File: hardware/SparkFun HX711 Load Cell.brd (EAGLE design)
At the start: 30.5 x 22.9 mm, 26 parts, among them Q1 MMBT4403, U1 HX711, U7 OSHW-LOGOS

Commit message: Silk label adjustment. Added cnt for shielding (yellow).
Some load cells have a 5th wire that is yellow that shields the four
wires. Added a ground connection for this 5th wire.
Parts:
- removed JP3: (no value), SparkFun-Connectors:1X04
- removed SJ1: (no value), SparkFun-Passives:PAD-JUMPER-2-NO_YES_SILK
- added JP4: (no value), SparkFun-Connectors:1X05
- added SJ2: (no value), SparkFun-Passives:PAD-JUMPER-2-NC_BY_TRACE_YES_SILK
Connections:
- net A+: now also JP4.2; no longer JP3.1
- net A-: now also JP4.3; no longer JP3.2
- net AVDD: now also JP4.5; no longer JP3.4
- net GND: now also JP4.1, JP4.4, SJ2.1; no longer JP3.3, SJ1.1
- net N$1: now also SJ2.2; no longer SJ1.2
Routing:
- net A-: track 7.56 -> 8.09 mm
- net A+: track 9.20 -> 9.73 mm
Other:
- board text added: "V02"
- board text added: "YLW"
- board text added: "YLW/SD"
- board text removed: "V01"
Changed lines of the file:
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@@
 <wire x1="30.48" y1="0" x2="0" y2="0" width="0.2032" layer="20"/>
 <wire x1="0" y1="0" x2="0" y2="22.86" width="0.2032" layer="20"/>
-<text x="3.048" y="6.985" size="1.27" layer="21" font="vector" ratio="15">GRN</text>
+<text x="3.048" y="8.255" size="1.27" layer="21" font="vector" ratio="15">GRN</text>
 <text x="5.334" y="1.27" size="1.778" layer="21" font="vector" ratio="15">Load Cell Amp</text>
-<text x="3.048" y="12.065" size="1.27" layer="21" font="vector" ratio="15">BLK</text>
-<text x="3.048" y="9.525" size="1.27" layer="21" font="vector" ratio="15">WHT</text>
-<text x="3.048" y="14.605" size="1.27" layer="21" font="vector" ratio="15">RED</text>
-<text x="9.398" y="6.985" size="1.27" layer="22" font="vector" ratio="15" rot="MR0">GRN/A+</text>
-<text x="9.398" y="9.525" size="1.27" layer="22" font="vector" ratio="15" rot="MR0">WHT/A-</text>
-<text x="9.398" y="12.065" size="1.27" layer="22" font="vector" ratio="15" rot="MR0">BLK/E-</text>
-<text x="9.398" y="14.605" size="1.27" layer="22" font="vector" ratio="15" rot="MR0">RED/E+</text>
-<text x="29.591" y="4.699" size="1.27" layer="16" font="vector" ratio="20" rot="MR0">V01</text>
+<text x="3.048" y="13.335" size="1.27" layer="21" font="vector" ratio="15">BLK</text>
+<text x="3.048" y="10.795" size="1.27" layer="21" font="vector" ratio="15">WHT</text>
+<text x="3.048" y="15.875" size="1.27" layer="21" font="vector" ratio="15">RED</text>
+<text x="9.398" y="8.255" size="1.27" layer="22" font="vector" ratio="15" rot="MR0">GRN/A+</text>
+<text x="9.398" y="10.795" size="1.27" layer="22" font="vector" ratio="15" rot="MR0">WHT/A-</text>
+<text x="9.398" y="13.335" size="1.27" layer="22" font="vector" ratio="15" rot="MR0">BLK/E-</text>
+<text x="9.398" y="15.875" size="1.27" layer="22" font="vector" ratio="15" rot="MR0">RED/E+</text>
+<text x="29.591" y="4.699" size="1.27" layer="16" font="vector" ratio="20" rot="MR0">V02</text>
 <text x="24.257" y="6.985" size="1.27" layer="21" font="vector" ratio="15">GND</text>
 <text x="24.257" y="12.065" size="1.27" layer="21" font="vector" ratio="15">DAT</text>
@@
 <dimension x1="1.27" y1="15.24" x2="29.21" y2="15.24" x3="15.24" y3="27.94" textsize="1.778" textratio="15" layer="47" unit="inch"/>
 <dimension x1="1.27" y1="7.62" x2="1.27" y2="0" x3="-7.62" y3="3.81" textsize="1.778" textratio="15" layer="47" unit="inch"/>
-<text x="20.955" y="14.605" size="1.27" layer="22" font="vector" ratio="15" rot="MR0">RATE</text>
+<text x="17.399" y="12.7" size="1.27" layer="22" font="vector" ratio="15" rot="MR0">RATE</text>
 <text x="19.685" y="6.985" size="1.27" layer="22" font="vector" ratio="15" rot="MR0">B+</text>
 <text x="19.685" y="4.445" size="1.27" layer="22" font="vector" ratio="15" rot="MR0">B-</text>
+<text x="3.048" y="5.715" size="1.27" layer="21" font="vector" ratio="15">YLW</text>
+<text x="9.398" y="5.715" size="1.27" layer="22" font="vector" ratio="15" rot="MR0">YLW/SD</text>
 </plain>
 <attributes>
@@
 <attribute name="PROD_ID" value="RES-00824" x="8.89" y="13.97" size="1.778" layer="27" font="vector" ratio="15" display="off"/>
 </element>
-<element name="JP3" library="SparkFun-Connectors" package="1X04" value="" x="1.27" y="7.62" rot="R90"/>
 <element name="R5" library="SparkFun-Resistors" package="0603-RES" value="10K" x="21.59" y="13.335" rot="R180">
 <attribute name="PROD_ID" value="RES-00824" x="21.59" y="13.335" size="1.778" layer="27" font="vector" ratio="15" rot="R180" display="off"/>
 </element>
-<element name="SJ1" library="SparkFun-Passives" package="PAD-JUMPER-2-NO_YES_SILK" value="" x="15.24" y="15.24" rot="MR180"/>
 <element name="C1" library="SparkFun-Capacitors" package="0603-CAP" value="0.1uF" x="8.89" y="6.35" rot="R180">
 <attribute name="PROD_ID" value="CAP-08604" x="8.89" y="6.35" size="1.778" layer="27" font="vector" ratio="15" rot="R180" display="off"/>
@@
 <element name="FID2" library="SparkFun-Aesthetics" package="FIDUCIAL-1X2" value="FIDUCIAL1X2" x="25.4" y="3.81"/>
 <element name="JP2" library="SparkFun-Connectors" package="1X02" value="M02PTH" x="21.59" y="7.62" rot="MR270"/>
+<element name="SJ2" library="SparkFun-Passives" package="PAD-JUMPER-2-NC_BY_TRACE_YES_SILK" value="" x="15.24" y="15.24" rot="MR180"/>
+<element name="JP4" library="SparkFun-Connectors" package="1X05" value="" x="1.27" y="6.35" rot="R90"/>
 </elements>
 <signals>
@@
 <contactref element="C7" pad="2"/>
 <contactref element="R2" pad="1"/>
-<contactref element="JP3" pad="3"/>
-<contactref element="SJ1" pad="1"/>
 <contactref element="C2" pad="1"/>
 <contactref element="C5" pad="2"/>
 <via x="22.86" y="16.51" extent="1-16" drill="0.508"/>
 <via x="22.86" y="21.59" extent="1-16" drill="0.508"/>
-<via x="15.24" y="12.7" extent="1-16" drill="0.508"/>
-<via x="15.24" y="10.16" extent="1-16" drill="0.508"/>
-<via x="15.24" y="7.62" extent="1-16" drill="0.508"/>
+<via x="15.24" y="11.43" extent="1-16" drill="0.508"/>
+<via x="15.24" y="8.89" extent="1-16" drill="0.508"/>
+<via x="15.24" y="6.35" extent="1-16" drill="0.508"/>
 <via x="15.24" y="21.59" extent="1-16" drill="0.508"/>
 <wire x1="18.288" y1="13.335" x2="18.542" y2="13.335" width="0.508" layer="1"/>
 <wire x1="18.542" y1="13.335" x2="18.923" y2="12.954" width="0.508" layer="1"/>
+<contactref element="SJ2" pad="1"/>
+<contactref element="JP4" pad="4"/>
+<contactref element="JP4" pad="1"/>
 </signal>
 <signal name="N$17">
@@
 <contactref element="U1" pad="3"/>
 <contactref element="R1" pad="2"/>
-<contactref element="JP3" pad="4"/>
 <wire x1="12.44" y1="13.335" x2="11.43" y2="13.335" width="0.254" layer="1"/>
 <wire x1="11.43" y1="13.335" x2="10.795" y2="13.97" width="0.254" layer="1"/>
 <wire x1="10.795" y1="13.97" x2="9.74" y2="13.97" width="0.254" layer="1"/>
-<wire x1="9.74" y1="13.97" x2="9.652" y2="13.97" width="0.254" layer="1"/>
-<wire x1="8.382" y1="15.24" x2="7.747" y2="15.24" width="0.254" layer="1"/>
-<wire x1="7.747" y1="15.24" x2="1.27" y2="15.24" width="0.254" layer="1"/>
-<wire x1="7.79" y1="16.51" x2="7.79" y2="15.283" width="0.254" layer="1"/>
 <wire x1="7.79" y1="16.51" x2="7.79" y2="19.22" width="0.254" layer="1"/>
 <wire x1="7.79" y1="19.22" x2="8.89" y2="20.32" width="0.254" layer="1"/>
 <wire x1="8.89" y1="20.32" x2="9.83" y2="20.32" width="0.254" layer="1"/>
-<wire x1="7.79" y1="15.283" x2="7.747" y2="15.24" width="0.254" layer="1"/>
-<wire x1="9.652" y1="13.97" x2="9.652" y2="14.605" width="0.254" layer="1"/>
-<wire x1="9.652" y1="14.605" x2="9.525" y2="14.732" width="0.254" layer="1"/>
-<wire x1="9.525" y1="14.732" x2="8.89" y2="14.732" width="0.254" layer="1"/>
-<wire x1="8.89" y1="14.732" x2="8.382" y2="15.24" width="0.254" layer="1"/>
+<contactref element="JP4" pad="5"/>
+<wire x1="7.79" y1="16.51" x2="1.27" y2="16.51" width="0.254" layer="1"/>
+<wire x1="9.74" y1="13.97" x2="9.74" y2="14.644" width="0.254" layer="1"/>
+<wire x1="9.74" y1="14.644" x2="9.652" y2="14.732" width="0.254" layer="1"/>
+<wire x1="9.652" y1="14.732" x2="8.128" y2="14.732" width="0.254" layer="1"/>
+<wire x1="8.128" y1="14.732" x2="7.79" y2="15.07" width="0.254" layer="1"/>
+<wire x1="7.79" y1="16.51" x2="7.79" y2="15.07" width="0.254" layer="1"/>
 </signal>
 <signal name="N$1">
 <contactref element="U1" pad="15"/>
 <contactref element="R5" pad="1"/>
-<contactref element="SJ1" pad="2"/>
 <wire x1="18.04" y1="14.605" x2="19.05" y2="14.605" width="0.254" layer="1"/>
 <via x="21.59" y="12.065" extent="1-16" drill="0.508"/>
-<wire x1="15.69" y1="15.24" x2="20.32" y2="15.24" width="0.254" layer="16"/>
 <wire x1="20.32" y1="15.24" x2="21.59" y2="13.97" width="0.254" layer="16"/>
 <wire x1="21.59" y1="13.97" x2="21.59" y2="12.065" width="0.254" layer="16"/>
@@
 <wire x1="22.44" y1="12.28" x2="22.225" y2="12.065" width="0.254" layer="1"/>
 <wire x1="22.225" y1="12.065" x2="21.59" y2="12.065" width="0.254" layer="1"/>
+<contactref element="SJ2" pad="2"/>
+<wire x1="15.748" y1="15.24" x2="20.32" y2="15.24" width="0.254" layer="16"/>
 </signal>
 <signal name="N$2">
@@
 </signal>
 <signal name="A-">
-<contactref element="JP3" pad="2"/>
 <contactref element="R3" pad="1"/>
 <wire x1="8.04" y1="8.255" x2="6.985" y2="8.255" width="0.254" layer="1"/>
-<wire x1="1.27" y1="10.16" x2="5.08" y2="10.16" width="0.254" layer="1"/>
-<wire x1="5.08" y1="10.16" x2="6.985" y2="8.255" width="0.254" layer="1"/>
+<wire x1="3.81" y1="11.43" x2="6.985" y2="8.255" width="0.254" layer="1"/>
+<contactref element="JP4" pad="3"/>
+<wire x1="1.27" y1="11.43" x2="3.81" y2="11.43" width="0.254" layer="1"/>
 </signal>
 <signal name="A+">
 <contactref element="R4" pad="1"/>
-<contactref element="JP3" pad="1"/>
 <wire x1="8.04" y1="4.445" x2="6.985" y2="4.445" width="0.254" layer="1"/>
 <wire x1="6.985" y1="4.445" x2="6.35" y2="5.08" width="0.254" layer="1"/>
 <wire x1="6.35" y1="5.08" x2="6.35" y2="6.985" width="0.254" layer="1"/>
 <wire x1="6.35" y1="6.985" x2="5.715" y2="7.62" width="0.254" layer="1"/>
-<wire x1="5.715" y1="7.62" x2="1.27" y2="7.62" width="0.254" layer="1"/>
+<contactref element="JP4" pad="2"/>
+<wire x1="1.27" y1="8.89" x2="4.445" y2="8.89" width="0.254" layer="1"/>
+<wire x1="4.445" y1="8.89" x2="5.715" y2="7.62" width="0.254" layer="1"/>
 </signal>
 <signal name="B+">

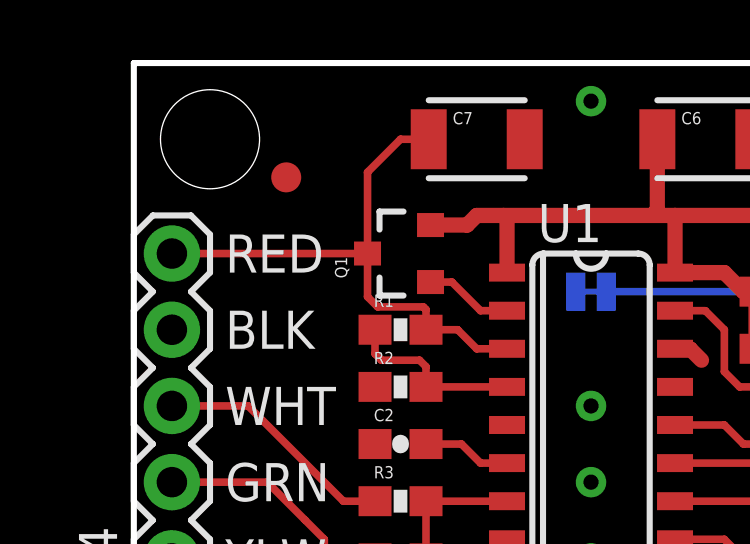
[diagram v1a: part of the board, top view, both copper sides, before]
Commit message: Change AVDD resistors to output closer to 5V
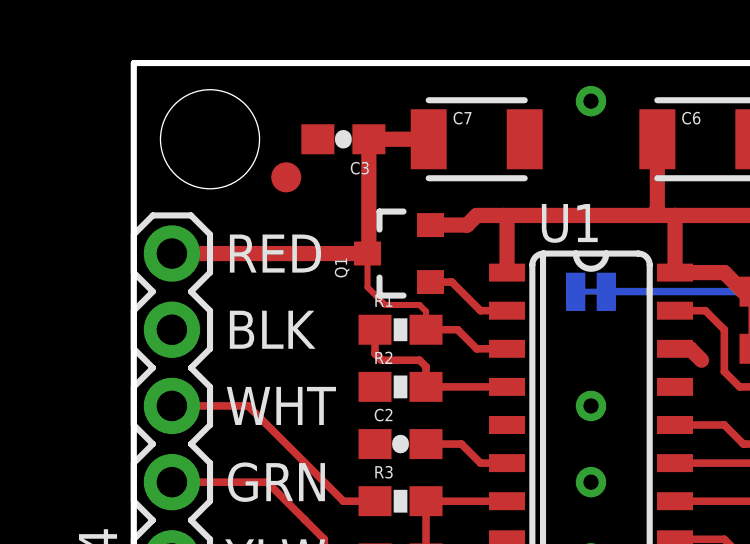
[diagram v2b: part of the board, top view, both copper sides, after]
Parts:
- added C3: 0.1uF, SparkFun-Capacitors:0603-CAP
- JP2: value M02PTH -> (none)
- R1: value 10K -> 20K
- R2: value 10K -> 8.2K
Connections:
- net AVDD: now also C3.1
- net GND: now also C3.2
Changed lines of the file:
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@@
 <grid distance="0.05" unitdist="inch" unit="inch" style="lines" multiple="1" display="yes" altdistance="0.005" altunitdist="inch" altunit="inch"/>
 <layers>
-<layer number="1" name="Top" color="4" fill="1" visible="yes" active="yes"/>
+<layer number="1" name="Top" color="4" fill="1" visible="no" active="yes"/>
 <layer number="2" name="Route2" color="1" fill="3" visible="no" active="no"/>
 <layer number="3" name="Route3" color="4" fill="3" visible="no" active="no"/>
@@
 <layer number="19" name="Unrouted" color="6" fill="1" visible="yes" active="yes"/>
 <layer number="20" name="Dimension" color="15" fill="1" visible="yes" active="yes"/>
-<layer number="21" name="tPlace" color="16" fill="1" visible="yes" active="yes"/>
+<layer number="21" name="tPlace" color="16" fill="1" visible="no" active="yes"/>
 <layer number="22" name="bPlace" color="14" fill="1" visible="yes" active="yes"/>
 <layer number="23" name="tOrigins" color="15" fill="1" visible="yes" active="yes"/>
@@
 <layer number="49" name="Reference" color="7" fill="1" visible="yes" active="yes"/>
 <layer number="50" name="dxf" color="7" fill="1" visible="no" active="no"/>
-<layer number="51" name="tDocu" color="6" fill="1" visible="yes" active="yes"/>
+<layer number="51" name="tDocu" color="6" fill="1" visible="no" active="yes"/>
 <layer number="52" name="bDocu" color="7" fill="1" visible="no" active="yes"/>
 <layer number="53" name="tGND_GNDA" color="7" fill="9" visible="no" active="no"/>
@@
 <dimension x1="27.94" y1="2.54" x2="2.54" y2="2.54" x3="15.24" y3="-5.08" textsize="1.778" textratio="15" layer="47" unit="inch"/>
 <dimension x1="1.27" y1="15.24" x2="29.21" y2="15.24" x3="15.24" y3="27.94" textsize="1.778" textratio="15" layer="47" unit="inch"/>
-<dimension x1="1.27" y1="7.62" x2="1.27" y2="0" x3="-7.62" y3="3.81" textsize="1.778" textratio="15" layer="47" unit="inch"/>
 <text x="17.399" y="12.7" size="1.27" layer="22" font="vector" ratio="15" rot="MR0">RATE</text>
 <text x="19.685" y="6.985" size="1.27" layer="22" font="vector" ratio="15" rot="MR0">B+</text>
@@
 <text x="3.048" y="5.715" size="1.27" layer="21" font="vector" ratio="15">YLW</text>
 <text x="9.398" y="5.715" size="1.27" layer="22" font="vector" ratio="15" rot="MR0">YLW/SD</text>
+<dimension x1="1.27" y1="6.35" x2="1.27" y2="0" x3="-8.89" y3="3.175" textsize="1.778" textratio="15" layer="47"/>
 </plain>
 <attributes>
@@
 <attribute name="PROD_ID" value="CAP-09824" x="11.43" y="20.32" size="1.778" layer="27" font="vector" ratio="15" display="off"/>
 </element>
-<element name="R2" library="SparkFun-Resistors" package="0603-RES" value="10K" x="8.89" y="12.065">
-<attribute name="PROD_ID" value="RES-00824" x="8.89" y="12.065" size="1.778" layer="27" font="vector" ratio="15" display="off"/>
-</element>
-<element name="R1" library="SparkFun-Resistors" package="0603-RES" value="10K" x="8.89" y="13.97">
-<attribute name="PROD_ID" value="RES-00824" x="8.89" y="13.97" size="1.778" layer="27" font="vector" ratio="15" display="off"/>
+<element name="R2" library="SparkFun-Resistors" package="0603-RES" value="8.2K" x="8.89" y="12.065">
+<attribute name="PROD_ID" value="RES-10646" x="8.89" y="12.065" size="1.778" layer="27" font="vector" ratio="15" display="off"/>
+</element>
+<element name="R1" library="SparkFun-Resistors" package="0603-RES" value="20K" x="8.89" y="13.97">
+<attribute name="PROD_ID" value="RES-09383" x="8.89" y="13.97" size="1.778" layer="27" font="vector" ratio="15" display="off"/>
 </element>
 <element name="R5" library="SparkFun-Resistors" package="0603-RES" value="10K" x="21.59" y="13.335" rot="R180">
@@
 <element name="FID1" library="SparkFun-Aesthetics" package="FIDUCIAL-1X2" value="FIDUCIAL1X2" x="5.08" y="19.05"/>
 <element name="FID2" library="SparkFun-Aesthetics" package="FIDUCIAL-1X2" value="FIDUCIAL1X2" x="25.4" y="3.81"/>
-<element name="JP2" library="SparkFun-Connectors" package="1X02" value="M02PTH" x="21.59" y="7.62" rot="MR270"/>
+<element name="JP2" library="SparkFun-Connectors" package="1X02" value="" x="21.59" y="7.62" rot="MR270"/>
 <element name="SJ2" library="SparkFun-Passives" package="PAD-JUMPER-2-NC_BY_TRACE_YES_SILK" value="" x="15.24" y="15.24" rot="MR180"/>
 <element name="JP4" library="SparkFun-Connectors" package="1X05" value="" x="1.27" y="6.35" rot="R90"/>
+<element name="C3" library="SparkFun-Capacitors" package="0603-CAP" value="0.1uF" x="6.985" y="20.32" rot="R180">
+<attribute name="PROD_ID" value="CAP-08604" x="6.985" y="20.32" size="1.778" layer="27" font="vector" ratio="15" rot="R180" display="off"/>
+</element>
 </elements>
 <signals>
@@
 <contactref element="JP4" pad="4"/>
 <contactref element="JP4" pad="1"/>
+<contactref element="C3" pad="2"/>
 </signal>
 <signal name="N$17">
@@
 <wire x1="11.43" y1="13.335" x2="10.795" y2="13.97" width="0.254" layer="1"/>
 <wire x1="10.795" y1="13.97" x2="9.74" y2="13.97" width="0.254" layer="1"/>
-<wire x1="7.79" y1="16.51" x2="7.79" y2="19.22" width="0.254" layer="1"/>
-<wire x1="7.79" y1="19.22" x2="8.89" y2="20.32" width="0.254" layer="1"/>
-<wire x1="8.89" y1="20.32" x2="9.83" y2="20.32" width="0.254" layer="1"/>
 <contactref element="JP4" pad="5"/>
-<wire x1="7.79" y1="16.51" x2="1.27" y2="16.51" width="0.254" layer="1"/>
-<wire x1="9.74" y1="13.97" x2="9.74" y2="14.644" width="0.254" layer="1"/>
-<wire x1="9.74" y1="14.644" x2="9.652" y2="14.732" width="0.254" layer="1"/>
-<wire x1="9.652" y1="14.732" x2="8.128" y2="14.732" width="0.254" layer="1"/>
-<wire x1="8.128" y1="14.732" x2="7.79" y2="15.07" width="0.254" layer="1"/>
-<wire x1="7.79" y1="16.51" x2="7.79" y2="15.07" width="0.254" layer="1"/>
+<wire x1="7.79" y1="16.51" x2="1.27" y2="16.51" width="0.508" layer="1"/>
+<contactref element="C3" pad="1"/>
+<wire x1="7.835" y1="20.32" x2="9.83" y2="20.32" width="0.508" layer="1"/>
+<wire x1="9.74" y1="13.97" x2="9.74" y2="14.5805" width="0.2032" layer="1"/>
+<wire x1="9.74" y1="14.5805" x2="9.525" y2="14.7955" width="0.2032" layer="1"/>
+<wire x1="9.525" y1="14.7955" x2="8.382" y2="14.7955" width="0.2032" layer="1"/>
+<wire x1="8.382" y1="14.7955" x2="7.79" y2="15.3875" width="0.2032" layer="1"/>
+<wire x1="7.79" y1="16.51" x2="7.79" y2="15.3875" width="0.2032" layer="1"/>
+<wire x1="7.835" y1="20.32" x2="7.835" y2="16.555" width="0.508" layer="1"/>
+<wire x1="7.835" y1="16.555" x2="7.79" y2="16.51" width="0.508" layer="1"/>
 </signal>
 <signal name="N$1">
@@
 </signal>
 </signals>
+<errors>
+</errors>
 </board>
 </drawing>

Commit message: Fixing issues #6.
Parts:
- FRAME1: value FRAME-LETTER -> (none)
- moved FRAME1 5.11 mm to (-5.08, -19.1)
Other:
- board text removed: "N. Seidle"
- board text removed: "V02"

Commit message: Fixed feedback from eng review.
Moved VCC trace out of tKeepout. Fixed 4-way junction on schematic.
Moved schematic part for standoff holes to proper location.
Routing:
- net VCC: track 32.6 -> 31.8 mm
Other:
- board text added: "Units are in inches"
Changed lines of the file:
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@@
 <?xml version="1.0" encoding="utf-8"?>
 <!DOCTYPE eagle SYSTEM "eagle.dtd">
-<eagle version="7.1.0">
+<eagle version="7.2.0">
 <drawing>
 <settings>
@@
 <text x="3.048" y="5.715" size="1.27" layer="21" font="vector" ratio="15">YLW</text>
 <text x="9.398" y="5.715" size="1.27" layer="22" font="vector" ratio="15" rot="MR0">YLW/SD</text>
-<dimension x1="1.27" y1="6.35" x2="1.27" y2="0" x3="-8.89" y3="3.175" textsize="1.778" textratio="15" layer="47"/>
+<dimension x1="1.27" y1="6.35" x2="1.27" y2="0" x3="-8.89" y3="3.175" textsize="1.778" textratio="15" layer="47" unit="inch"/>
+<text x="1.27" y="-10.033" size="1.778" layer="47">Units are in inches</text>
 </plain>
 <attributes>
@@
 <contactref element="R5" pad="2"/>
 <contactref element="C5" pad="1"/>
-<wire x1="29.21" y1="15.24" x2="29.21" y2="16.51" width="0.508" layer="1"/>
-<wire x1="29.21" y1="16.51" x2="27.94" y2="17.78" width="0.508" layer="1"/>
-<wire x1="27.94" y1="17.78" x2="18.034" y2="17.78" width="0.508" layer="1"/>
 <wire x1="18.034" y1="17.78" x2="17.272" y2="17.78" width="0.508" layer="1"/>
 <wire x1="17.272" y1="17.78" x2="12.319" y2="17.78" width="0.508" layer="1"/>
@@
 <wire x1="17.45" y1="20.32" x2="17.45" y2="17.958" width="0.508" layer="1"/>
 <wire x1="17.45" y1="17.958" x2="17.272" y2="17.78" width="0.508" layer="1"/>
+<wire x1="29.21" y1="15.24" x2="26.67" y2="15.24" width="0.508" layer="1"/>
+<wire x1="26.67" y1="15.24" x2="24.13" y2="17.78" width="0.508" layer="1"/>
+<wire x1="24.13" y1="17.78" x2="18.034" y2="17.78" width="0.508" layer="1"/>
 </signal>
 <signal name="DAT">
